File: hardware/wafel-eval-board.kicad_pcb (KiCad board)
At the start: 2 copper layers, 237 parts, among them J101 CAN PORT, J102 SW, J801 UART1, Q1001 DMG2302UK, Q1101 DMG2302UK, Q1201 DMG2302UK, Q1301 DMG2302UK, Q1401 DMG2302UK, Q1501 DMG2302UK, Q1601 DMG2302UK, Q1701 DMG2302UK, Q1801 DMG2302UK, Q1901 DMG2302UK, Q201 NPN, Q202 2N7002, Q301 IRLML6402, Q302 2N7002, Q401 IPB085N15NM6, Q402 IPB085N15NM6, Q403 IPB085N15NM6, Q501 IPB085N15NM6, Q502 IPB085N15NM6, Q503 IPB085N15NM6, Q601 PMOS, Q701 PMOS, Q901 ZXMP10A13FTA, Q902 BSS123, SW801 SW_Push, U101 LM5163DDA, U201 BQ7694204, U801 NUCLEO-L432KC, U803 TLP241A

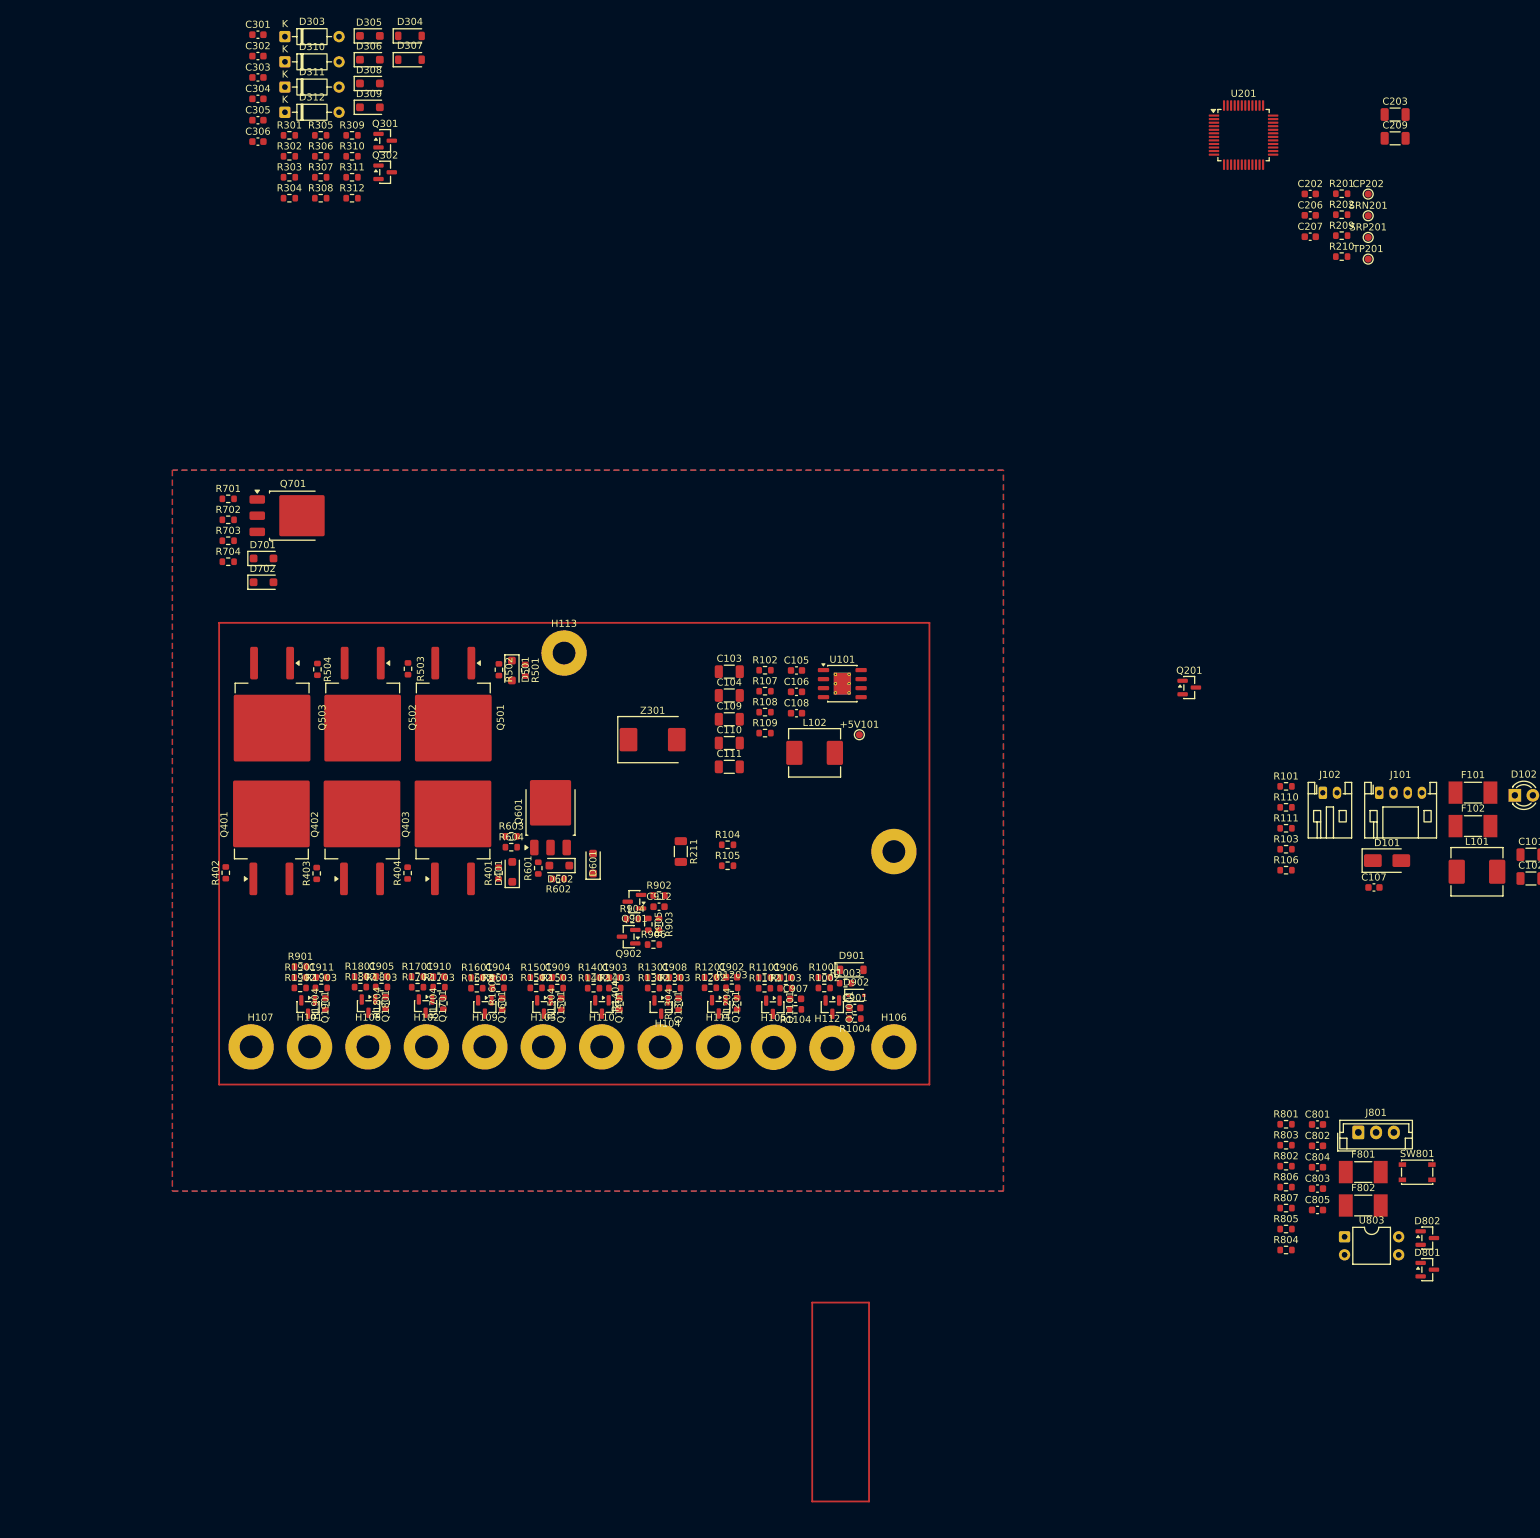
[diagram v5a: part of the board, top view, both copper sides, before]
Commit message: reduced BOM
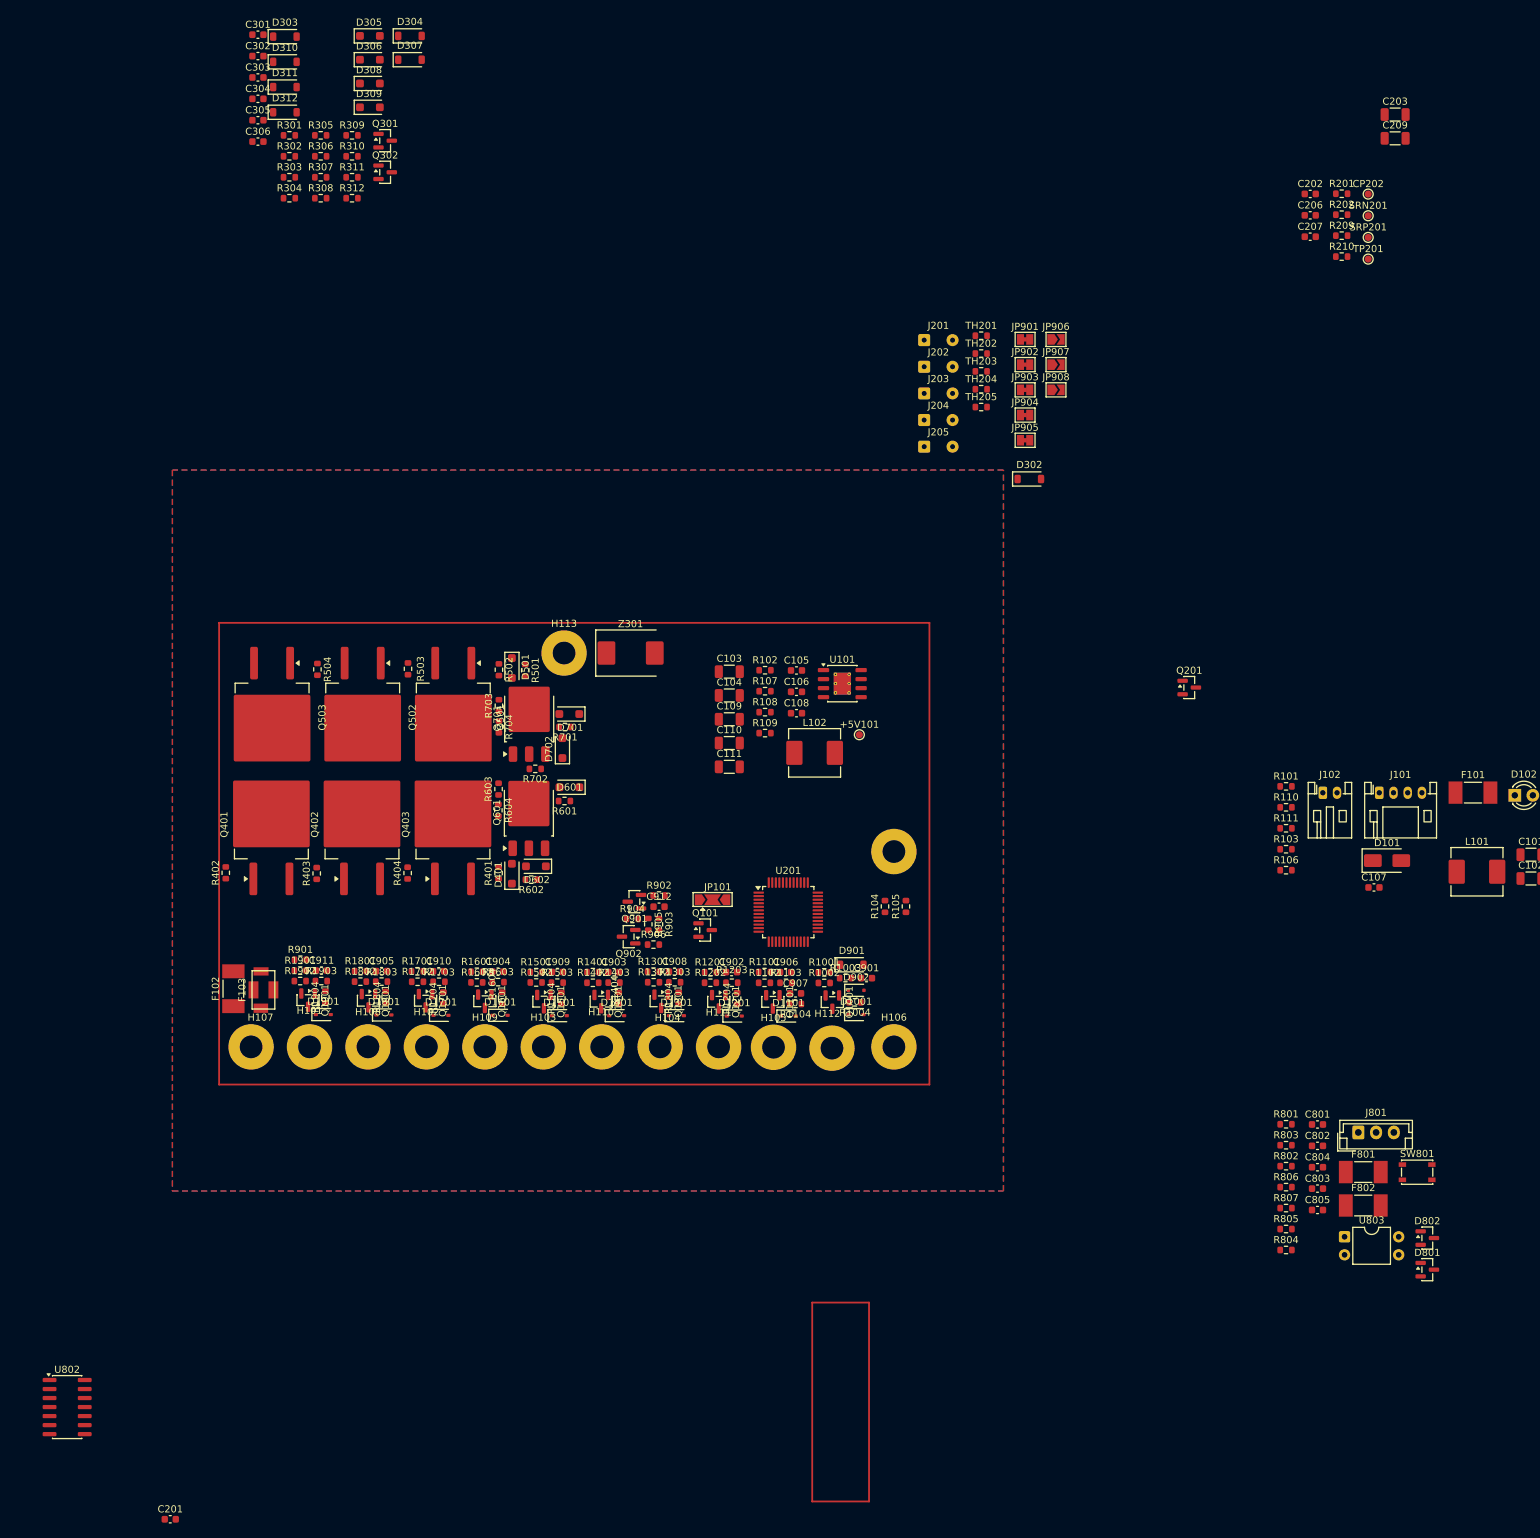
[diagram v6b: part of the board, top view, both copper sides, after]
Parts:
- removed R211: 1m, Resistor_SMD:R_1206_3216Metric
- added C201: 10n, Capacitor_SMD:C_0603_1608Metric, F.Cu at (51.6, 173.0)
- added D1001: BZT52C5V6S, Diode_SMD:D_SOD-323, F.Cu at (148.2, 102.0)
- added D1101: BZT52C5V6S, Diode_SMD:D_SOD-323, F.Cu at (138.6, 102.2)
- added D1201: BZT52C5V6S, Diode_SMD:D_SOD-323, F.Cu at (131.0, 102.2)
- added D1301: BZT52C5V6S, Diode_SMD:D_SOD-323, F.Cu at (122.9, 102.1)
- added D1401: BZT52C5V6S, Diode_SMD:D_SOD-323, F.Cu at (114.5, 102.1)
- added D1501: BZT52C5V6S, Diode_SMD:D_SOD-323, F.Cu at (106.4, 102.1)
- added D1601: BZT52C5V6S, Diode_SMD:D_SOD-323, F.Cu at (98.1, 102.1)
- added D1701: BZT52C5V6S, Diode_SMD:D_SOD-323, F.Cu at (89.7, 102.1)
- added D1801: BZT52C5V6S, Diode_SMD:D_SOD-323, F.Cu at (81.7, 102.0)
- added D1901: BZT52C5V6S, Diode_SMD:D_SOD-323, F.Cu at (73.2, 102.0)
- added D302: BZT52B5V1, Diode_SMD:D_SOD-123, F.Cu at (172.6, 26.5)
- added F103: Fuse_3Terminal, wafel-eval-board:Fuse_ITV5432, F.Cu at (64.7, 98.5)
- added J201: Conn_01x02, Connector_Wire:SolderWire-0.15sqmm_1x02_P4mm_D0.5mm_OD1.5mm, F.Cu at (157.8, 7.00)
- added J202: Conn_01x02, Connector_Wire:SolderWire-0.15sqmm_1x02_P4mm_D0.5mm_OD1.5mm, F.Cu at (157.8, 10.7)
- added J203: Conn_01x02, Connector_Wire:SolderWire-0.15sqmm_1x02_P4mm_D0.5mm_OD1.5mm, F.Cu at (157.8, 14.5)
- added J204: Conn_01x02, Connector_Wire:SolderWire-0.15sqmm_1x02_P4mm_D0.5mm_OD1.5mm, F.Cu at (157.8, 18.2)
- added J205: Conn_01x02, Connector_Wire:SolderWire-0.15sqmm_1x02_P4mm_D0.5mm_OD1.5mm, F.Cu at (157.8, 22.0)
- added JP101: SJ3O, Jumper:SolderJumper-3_P2.0mm_Open_TrianglePad1.0x1.5mm, F.Cu at (128.0, 85.8)
- added JP901: SolderJumper_2_Bridged, Jumper:SolderJumper-2_P1.3mm_Bridged_Pad1.0x1.5mm, F.Cu at (172.0, 6.90)
- added JP902: SolderJumper_2_Bridged, Jumper:SolderJumper-2_P1.3mm_Bridged_Pad1.0x1.5mm, F.Cu at (172.0, 10.4)
- added JP903: SolderJumper_2_Bridged, Jumper:SolderJumper-2_P1.3mm_Bridged_Pad1.0x1.5mm, F.Cu at (172.0, 14.0)
- added JP904: SolderJumper_2_Bridged, Jumper:SolderJumper-2_P1.3mm_Bridged_Pad1.0x1.5mm, F.Cu at (172.0, 17.5)
- added JP905: SolderJumper_2_Bridged, Jumper:SolderJumper-2_P1.3mm_Bridged_Pad1.0x1.5mm, F.Cu at (172.0, 21.1)
- added JP906: SolderJumper_2_Open, Jumper:SolderJumper-2_P1.3mm_Open_TrianglePad1.0x1.5mm, F.Cu at (176.3, 6.90)
- added JP907: SolderJumper_2_Open, Jumper:SolderJumper-2_P1.3mm_Open_TrianglePad1.0x1.5mm, F.Cu at (176.3, 10.4)
- added JP908: SolderJumper_2_Open, Jumper:SolderJumper-2_P1.3mm_Open_TrianglePad1.0x1.5mm, F.Cu at (176.3, 14.0)
- added Q101: AO3422, Package_TO_SOT_SMD:SOT-23, F.Cu at (126.9, 90.1)
- added TH201: 10k, Resistor_SMD:R_0603_1608Metric, F.Cu at (165.8, 6.38)
- added TH202: 10k, Resistor_SMD:R_0603_1608Metric, F.Cu at (165.8, 8.89)
- added TH203: 10k, Resistor_SMD:R_0603_1608Metric, F.Cu at (165.8, 11.4)
- added TH204: 10k, Resistor_SMD:R_0603_1608Metric, F.Cu at (165.8, 13.9)
- added TH205: 10k, Resistor_SMD:R_0603_1608Metric, F.Cu at (165.8, 16.4)
- added U802: TCAN1043A, Package_SO:SOIC-14_3.9x8.7mm_P1.27mm, F.Cu at (37.1, 157.2)
- C301, C302, C303, C304, C305, C306, C802, C804, C805: value 0.1u -> 100n
- C801: value 470u -> 470n
- D303, D310, D311, D312: value BAT46 -> BAT46W; footprint Diode_THT:D_DO-35_SOD27_P7.62mm_Horizontal -> Diode_SMD:D_SOD-123
- D306: value BZT52Bxx -> BZT52B16
- Q202, Q302: value 2N7002 -> DMG2302UK
- Q601, Q701: value PMOS -> IRFR9024
- Q902: value BSS123 -> DMG2302UK
- R1001, R1002, R1004, R1101, R1102, R1104, R1201, R1202, R1204, R1301, R1302, R1304, R1401, R1402, R1404, R1501, R1502, R1504, R1601, R1602, R1604, R1701, R1702, R1704, R1801, R1802, R1804, R1901, R1902, R1904: value 100R -> 100
- R203, R204: value 10K -> 10k
- R208: value 50k -> 49.9k
- R303, R304: value 5.1K -> 5.1k
- moved F102 176.0 mm to (60.5, 98.3), turned to 90 degrees
- moved U201 126.8 mm to (138.6, 87.5)
- moved R701 57.3 mm to (107.2, 61.5), turned to 180 degrees
- moved R702 55.7 mm to (103.0, 67.4), turned to 180 degrees
- moved D701 48.3 mm to (107.8, 59.6), turned to 180 degrees
- moved D702 48.1 mm to (106.8, 64.4), turned to 90 degrees
- moved R704 44.7 mm to (97.9, 61.5), turned to -90 degrees
- moved R703 44.6 mm to (97.9, 58.5), turned to 90 degrees
- moved Q701 43.8 mm to (102.2, 60.2), turned to 90 degrees
- moved R105 25.8 mm to (155.2, 86.7), turned to 90 degrees
- moved R104 23.8 mm to (152.2, 86.7), turned to 90 degrees
- moved Z301 12.6 mm to (116.4, 51.1)
- moved D601 11.2 mm to (107.8, 70.0), turned to 180 degrees
- moved R601 10.1 mm to (107.1, 71.9), turned to 180 degrees
- moved R603 6.89 mm to (97.8, 70.2), turned to 90 degrees
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
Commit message: reduced BOM
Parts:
- moved U801 125.1 mm to (171.6, 79.8)
- moved C301 122.0 mm to (75.7, 85.4), turned to -90 degrees
- moved C302 116.0 mm to (75.7, 82.4), turned to -90 degrees
- moved D301 107.1 mm to (61.4, 76.4), turned to 90 degrees
- moved R703 6.97 mm to (101.4, 64.5)
- moved R403 4.42 mm to (75.7, 79.4)
- moved R402 3.51 mm to (62.9, 82.0)
- moved D401 3.51 mm to (103.2, 82.1)
- moved D501 3.51 mm to (103.2, 53.2)
- moved D601 3.51 mm to (111.3, 70.0)
- moved D602 3.51 mm to (106.6, 81.1)
- moved D701 3.51 mm to (111.3, 59.6)
- moved Q401 3.51 mm to (69.4, 75.2)
- moved Q402 3.51 mm to (82.1, 75.2)
- moved Q501 3.51 mm to (95.0, 60.1)
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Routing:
- net /CH: track 0.00 -> 161.4 mm
- net /BAT+: track 0.00 -> 90.1 mm
- net /High-Side N-MOSFET/MOSFET-CASCADE-CHG/GATE: track 0.00 -> 41.9 mm
- net /CB Mosfets/CELL10: track 0.00 -> 33.5 mm
- net /CB Mosfets/CELL8: track 0.00 -> 30.9 mm
- net /CB Mosfets/CELL4: track 0.00 -> 28.8 mm
- net /CB Mosfets/CELL9: track 0.00 -> 28.6 mm
- net /CB Mosfets/CELL7: track 0.00 -> 28.1 mm
- net /CB Mosfets/CELL6: track 0.00 -> 28.1 mm
- net /CB Mosfets/CELL5: track 0.00 -> 27.9 mm
- net /CB Mosfets/CELL3: track 0.00 -> 27.6 mm
- net /CB Mosfets/CELL2: track 0.00 -> 26.7 mm
- net /CB Mosfets/CELL1: track 0.00 -> 20.9 mm
- net /CB Mosfets/CELL0: track 0.00 -> 16.2 mm
- net /CB Mosfets/VC9: track 0.00 -> 10.6 mm
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
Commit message: increased size two times
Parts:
- removed C904, C905, C910: 220n, Capacitor_SMD:C_0603_1608Metric
- removed JP901, JP902, JP903, JP904, JP905: SolderJumper_2_Bridged, Jumper:SolderJumper-2_P1.3mm_Bridged_Pad1.0x1.5mm
- removed JP906, JP907, JP908: SolderJumper_2_Open, Jumper:SolderJumper-2_P1.3mm_Open_TrianglePad1.0x1.5mm
- added R907: 0, Resistor_SMD:R_0603_1608Metric, F.Cu at (97.8, 96.0)
- added R908: 0, Resistor_SMD:R_0603_1608Metric, F.Cu at (89.4, 95.9)
- added R909: 0, Resistor_SMD:R_0603_1608Metric, F.Cu at (81.4, 95.8)
- JP101: footprint Jumper:SolderJumper-3_P2.0mm_Open_TrianglePad1.0x1.5mm -> Jumper:SolderJumper-3_P1.3mm_Open_Pad1.0x1.5mm
- moved C303 214.6 mm to (247.1, 81.8), turned to 90 degrees
- moved C205 211.9 mm to (125.0, 67.5)
- moved C304 211.5 mm to (247.1, 78.8), turned to 90 degrees
- moved C101 199.8 mm to (44.3, 60.4)
- moved C102 199.8 mm to (44.3, 63.7)
- moved C107 199.8 mm to (22.2, 65.0)
- moved D101 199.8 mm to (24.0, 61.2)
- moved D801 199.8 mm to (29.7, 118.8)
- moved D802 199.8 mm to (29.7, 114.4)
- moved F101 199.8 mm to (36.1, 51.6)
- moved J101 199.8 mm to (22.9, 51.7)
- moved L101 199.8 mm to (36.7, 62.8)
- moved Q201 199.8 mm to (-3.82, 36.8)
- moved R101 199.8 mm to (9.80, 50.8)
- moved R103 199.8 mm to (9.80, 59.6)
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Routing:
- net /CH: track 161.4 -> 6.07 mm
- net /BAT+: track 90.1 -> 1.61 mm
- net Net-(F103-Pad4): track 0.00 -> 60.6 mm
- net /CB Mosfets/VC10: track 2.09 -> 59.7 mm
- net /CB Mosfets/VC9: track 10.6 -> 60.2 mm
- net /CB Mosfets/CELL10: track 33.5 -> 79.5 mm
- net /CB Mosfets/VC8: track 10.0 -> 52.1 mm
- net /CB Mosfets/VC7: track 10.4 -> 44.6 mm
- net /CB Mosfets/VC6: track 10.4 -> 37.1 mm
- net /CB Mosfets/VC5: track 10.1 -> 29.6 mm
- net /High-Side N-MOSFET/MOSFET-CASCADE-CHG/GATE: track 41.9 -> 27.8 mm
- net /CB Mosfets/VC3: track 3.05 -> 15.9 mm
- net /CB Mosfets/VC4: track 10.5 -> 22.1 mm
- net /CB Mosfets/VC0: track 7.90 -> 15.4 mm
- net Net-(Q701-D): track 4.03 -> 0.00 mm
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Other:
- board text added: "PWZ+"
- board text added: "PWZ-"
